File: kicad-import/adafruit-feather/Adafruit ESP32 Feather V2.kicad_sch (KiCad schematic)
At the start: 59 parts

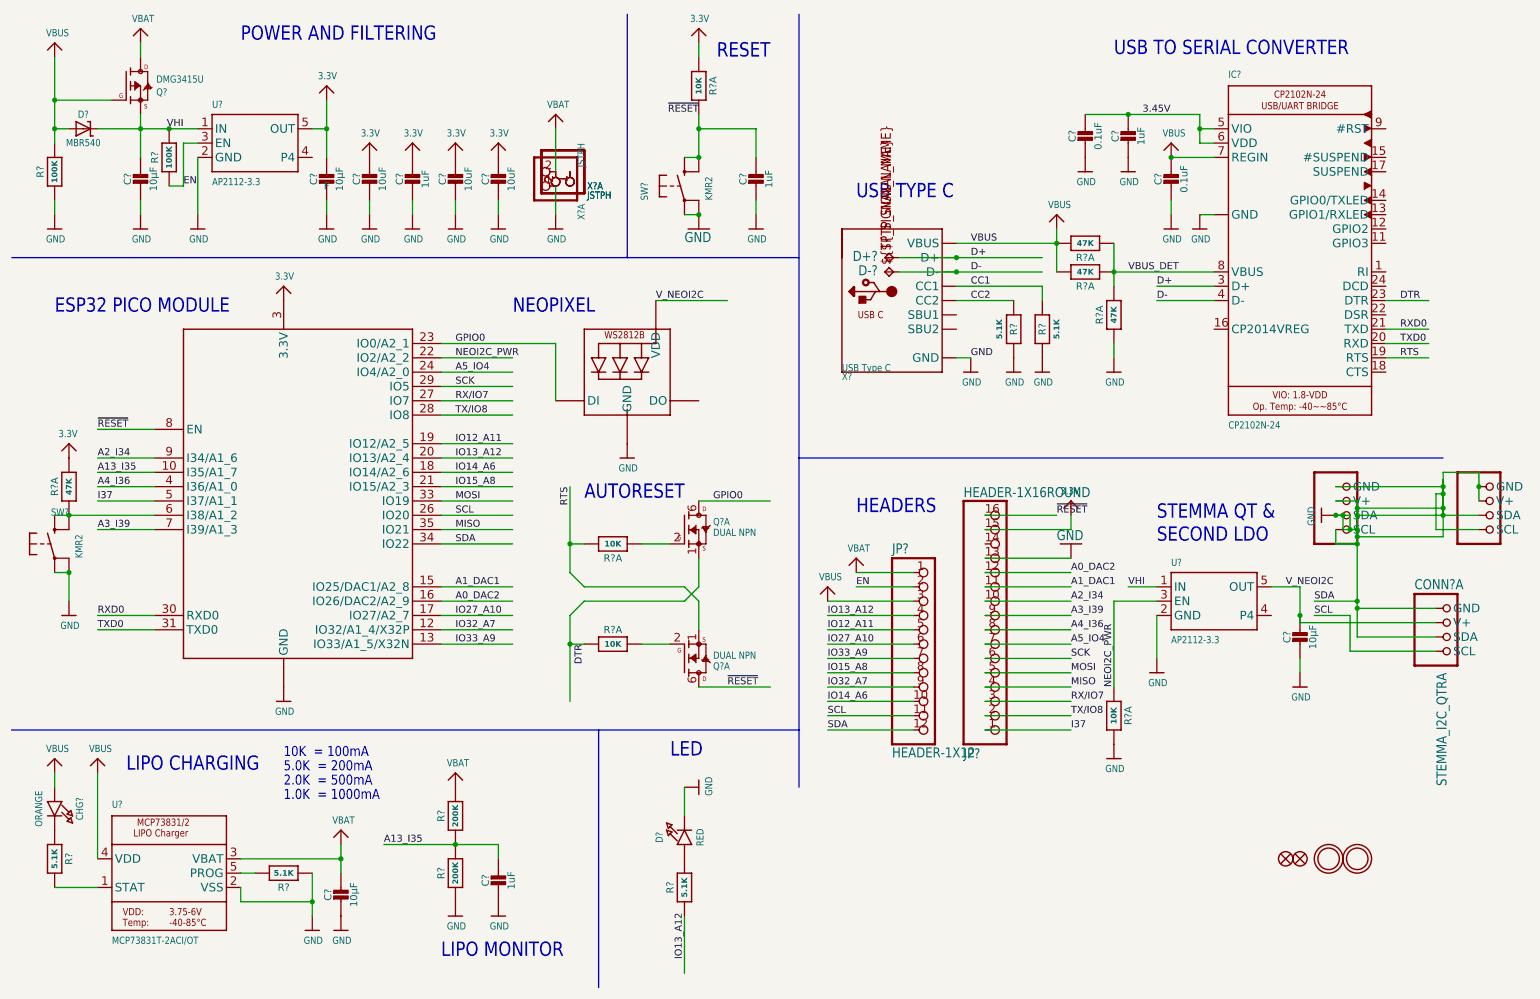
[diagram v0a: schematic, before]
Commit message: Remove Stemma QT connectors and LiPo circuitry. Update Notes.
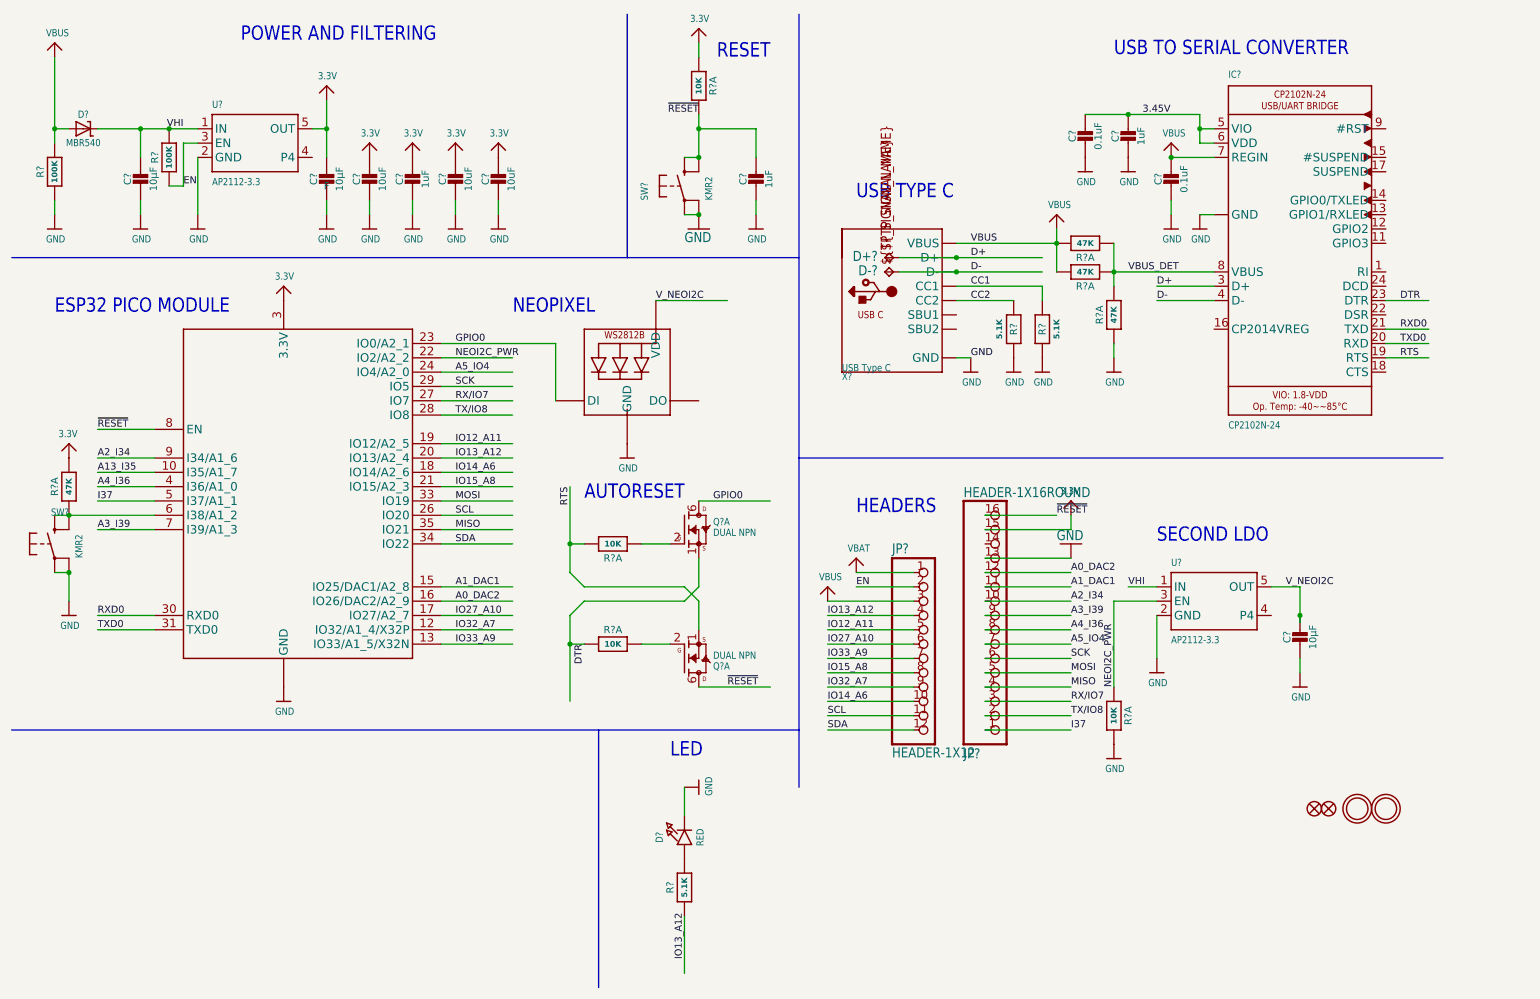
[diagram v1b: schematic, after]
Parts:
- removed C?: 1uF, Adafruit ESP32 Feather V2:0603-NO, symbol Adafruit ESP32 Feather V2-eagle-import:CAP_CERAMIC0603_NO
- removed C?: 10µF, Adafruit ESP32 Feather V2:0805-NO, symbol Adafruit ESP32 Feather V2-eagle-import:CAP_CERAMIC0805-NOOUTLINE
- removed CHG?: ORANGE, Adafruit ESP32 Feather V2:CHIPLED_0603_NOOUTLINE, symbol Adafruit ESP32 Feather V2-eagle-import:LED0603_NOOUTLINE
- removed CONN? (x3): STEMMA_I2C_QTRA, Adafruit ESP32 Feather V2:JST_SH4_RA, symbol Adafruit ESP32 Feather V2-eagle-import:STEMMA_I2C_QTRA
- removed Q?: DMG3415U, Adafruit ESP32 Feather V2:SOT23-R, symbol Adafruit ESP32 Feather V2-eagle-import:MOSFET-P
- removed R? (x2): 200K, Adafruit ESP32 Feather V2:0603-NO, symbol Adafruit ESP32 Feather V2-eagle-import:RESISTOR_0603_NOOUT
- removed R? (x2): 5.1K, Adafruit ESP32 Feather V2:0603-NO, symbol Adafruit ESP32 Feather V2-eagle-import:RESISTOR_0603_NOOUT
- removed U?: MCP73831T-2ACI/OT, Adafruit ESP32 Feather V2:SOT23-5, symbol Adafruit ESP32 Feather V2-eagle-import:MCP73831/2
- removed X? (x3): JSTPH, Adafruit ESP32 Feather V2:JSTPH2_BATT, symbol Adafruit ESP32 Feather V2-eagle-import:CON_JST_PH_2PIN_MT_BATT
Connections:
- net GND: no longer JP?.12, X?.34 (IO22)
- new net SDA: JP?.12, X?.34 (IO22)
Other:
- note added: "SECOND LDO"
- note removed: "1.0K = 1000mA"
- note removed: "10K = 100mA"
- note removed: "2.0K = 500mA"
- note removed: "5.0K = 200mA"
- note removed: "LIPO CHARGING"
- note removed: "LIPO MONITOR"
- note removed: "STEMMA QT & SECOND LDO"

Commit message: Add initial annotation.
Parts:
- gave numbers to parts that had none: 44

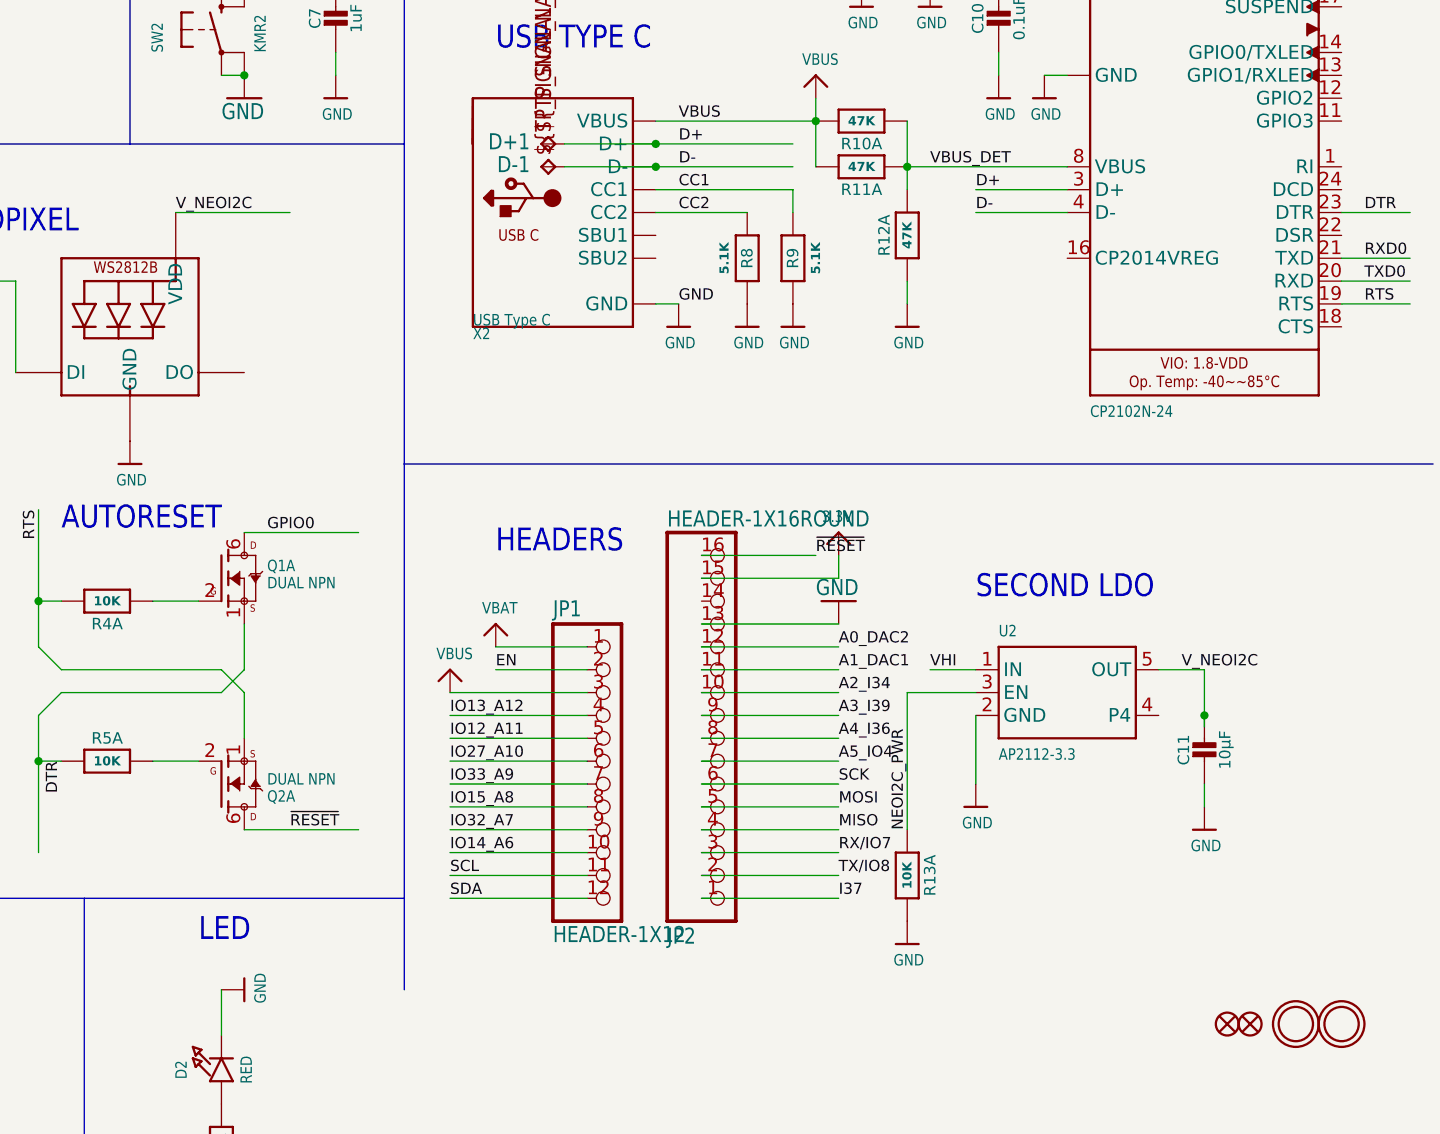
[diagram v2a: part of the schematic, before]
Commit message: Remove second LDO. Power Neopixel from main 3.3.
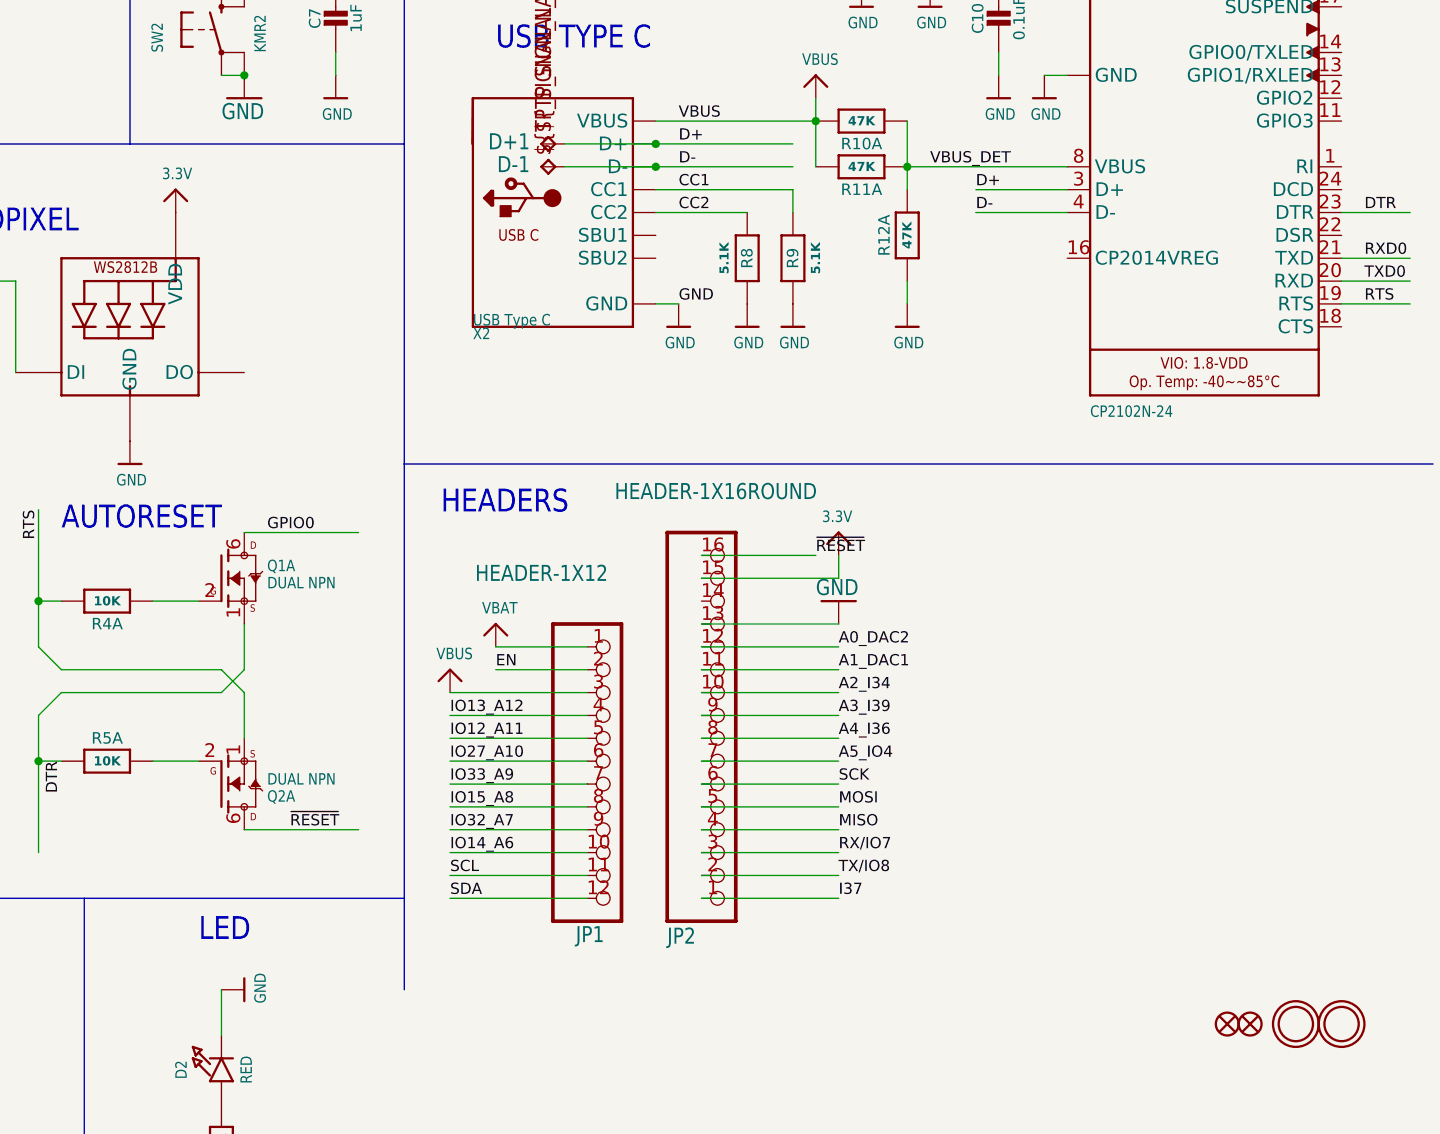
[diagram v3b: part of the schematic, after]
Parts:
- removed C11: 10µF, Adafruit ESP32 Feather V2:0805-NO, symbol Adafruit ESP32 Feather V2-eagle-import:CAP_CERAMIC0805-NOOUTLINE
- removed R13: 10K, Adafruit ESP32 Feather V2:RESPACK_4X0603, symbol Adafruit ESP32 Feather V2-eagle-import:RESISTOR_4PACK
- removed U2: AP2112-3.3, Adafruit ESP32 Feather V2:SOT23-5, symbol Adafruit ESP32 Feather V2-eagle-import:VREG_SOT23-5
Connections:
- net V_NEOI2C is gone; now on net 3.3V: LED1.2 (VDD)
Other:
- note removed: "SECOND LDO"

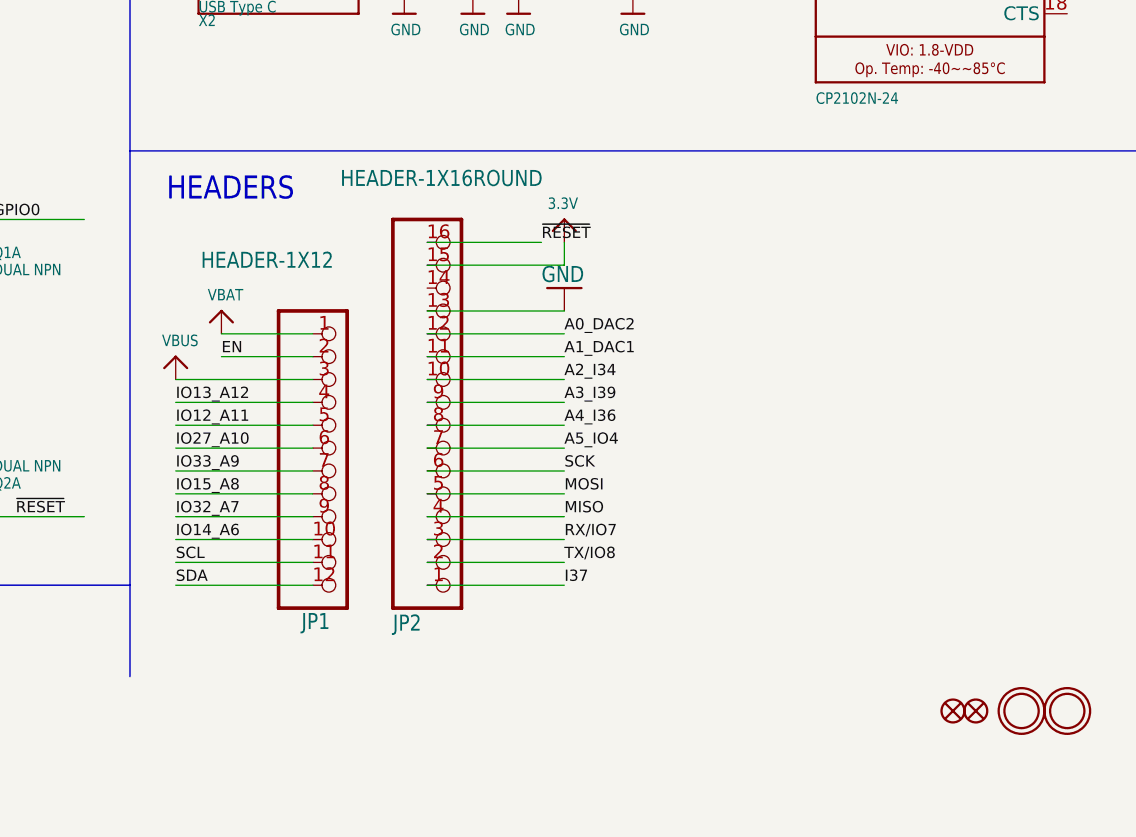
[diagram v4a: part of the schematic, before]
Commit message: Start adding heirarchical labels. Add notes to check sub-feather jumpers.
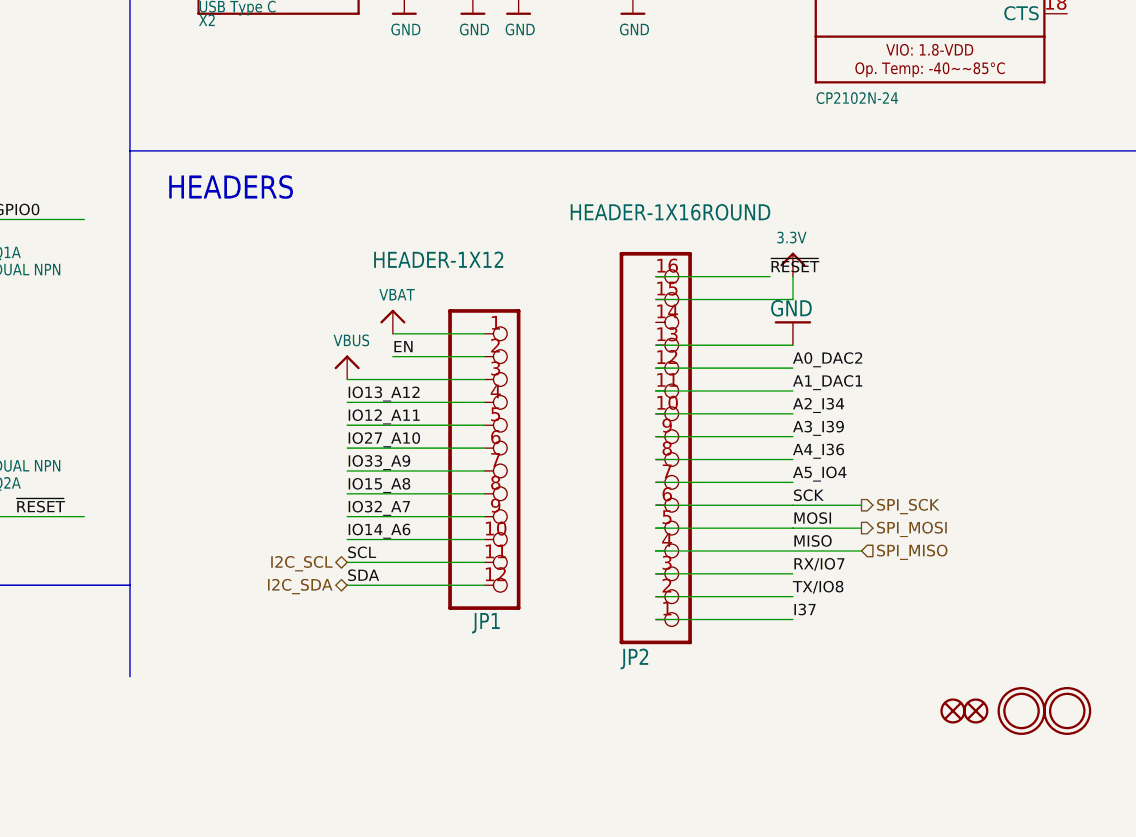
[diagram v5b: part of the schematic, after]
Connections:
- net MISO renamed SPI_MISO
- net MOSI renamed SPI_MOSI
- net SCK renamed SPI_SCK
- net SCL renamed I2C_SCL
- net SDA renamed I2C_SDA
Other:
- moved on the sheet: JP1, JP2

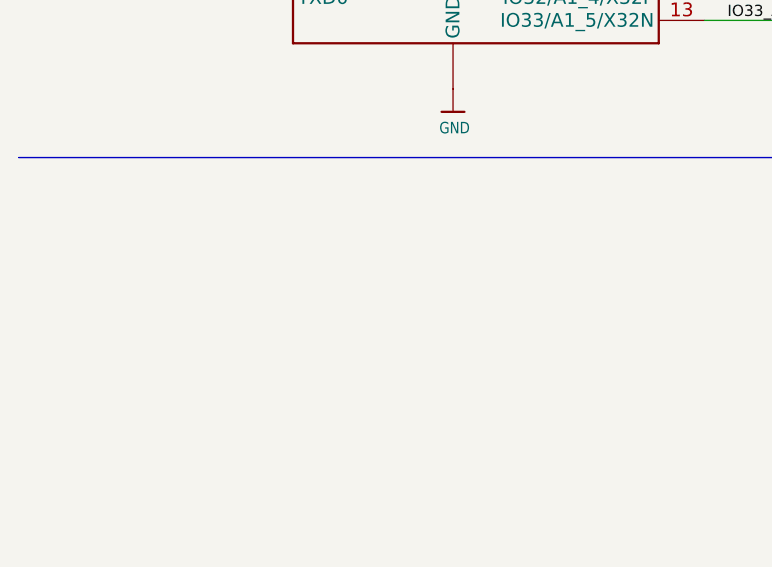
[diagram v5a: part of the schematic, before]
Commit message: Add cross-sheet nets for I2C.
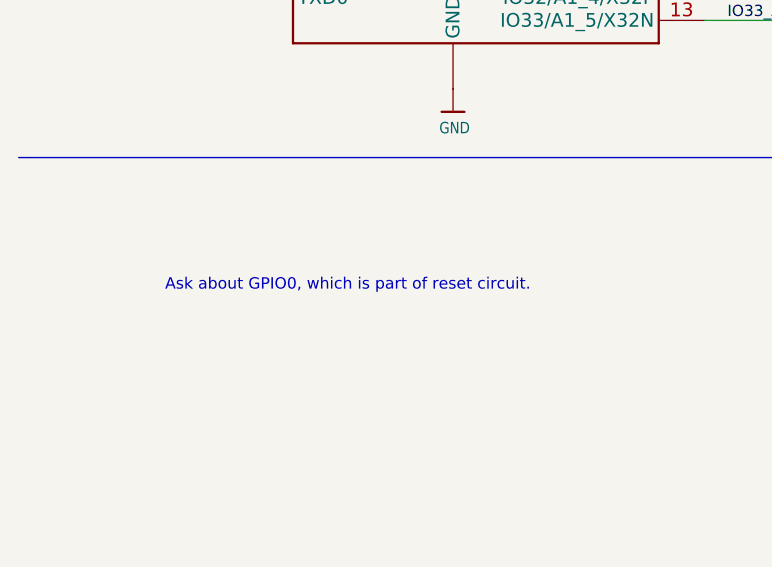
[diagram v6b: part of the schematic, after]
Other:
- note added: "Ask about GPIO0, which is part of reset circuit."
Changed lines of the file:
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@@
+		)
+	)
+	(text "Ask about GPIO0, which is part of reset circuit."
+		(exclude_from_sim no)
+		(at 56.896 164.084 0)
+		(effects
+			(font
+				(size 1.27 1.27)
+			)
 		)
 	)

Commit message: Initial sheet settings for layout.
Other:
- company: (none) -> Kingdom Metrics
- title: (none) -> Genesis Board
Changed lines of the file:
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@@
 	(generator_version "9.0")
 	(paper "User" 303.962 217.322)
+	(title_block
+		(title "Genesis Board")
+		(date "2025-05-27")
+		(rev "0.1")
+		(company "Kingdom Metrics")
+	)
 	(text "HEADERS"
 		(exclude_from_sim no)
